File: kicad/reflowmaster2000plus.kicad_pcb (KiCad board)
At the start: 2 copper layers, 46.6 x 24.1 mm, 21 parts, among them IC1 TLP3063, P1 CONN_8, P2 Toaster, P3 220V, U1 TRIAC, U2 TLC2272

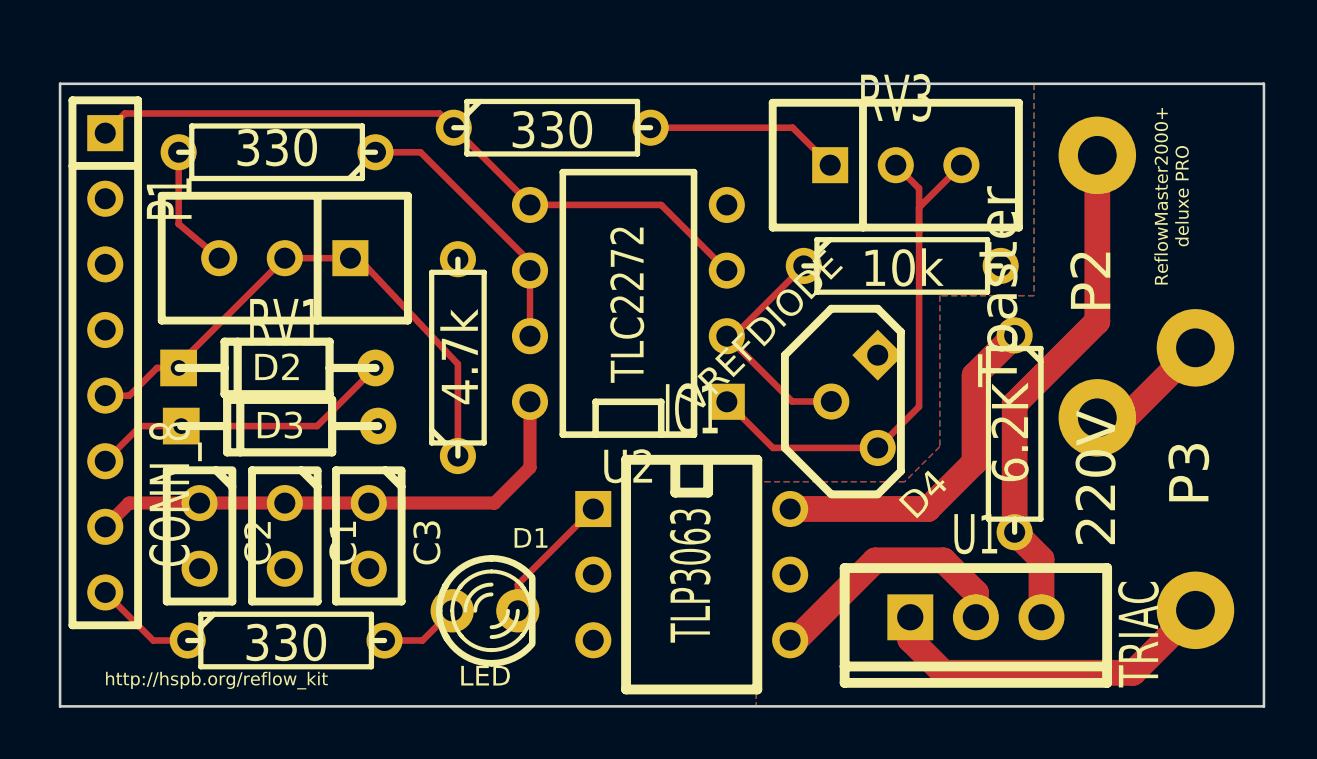
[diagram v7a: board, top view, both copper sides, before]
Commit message: SCH and PCB almost completely redrawn. Moved symbols and components to a separate lib.
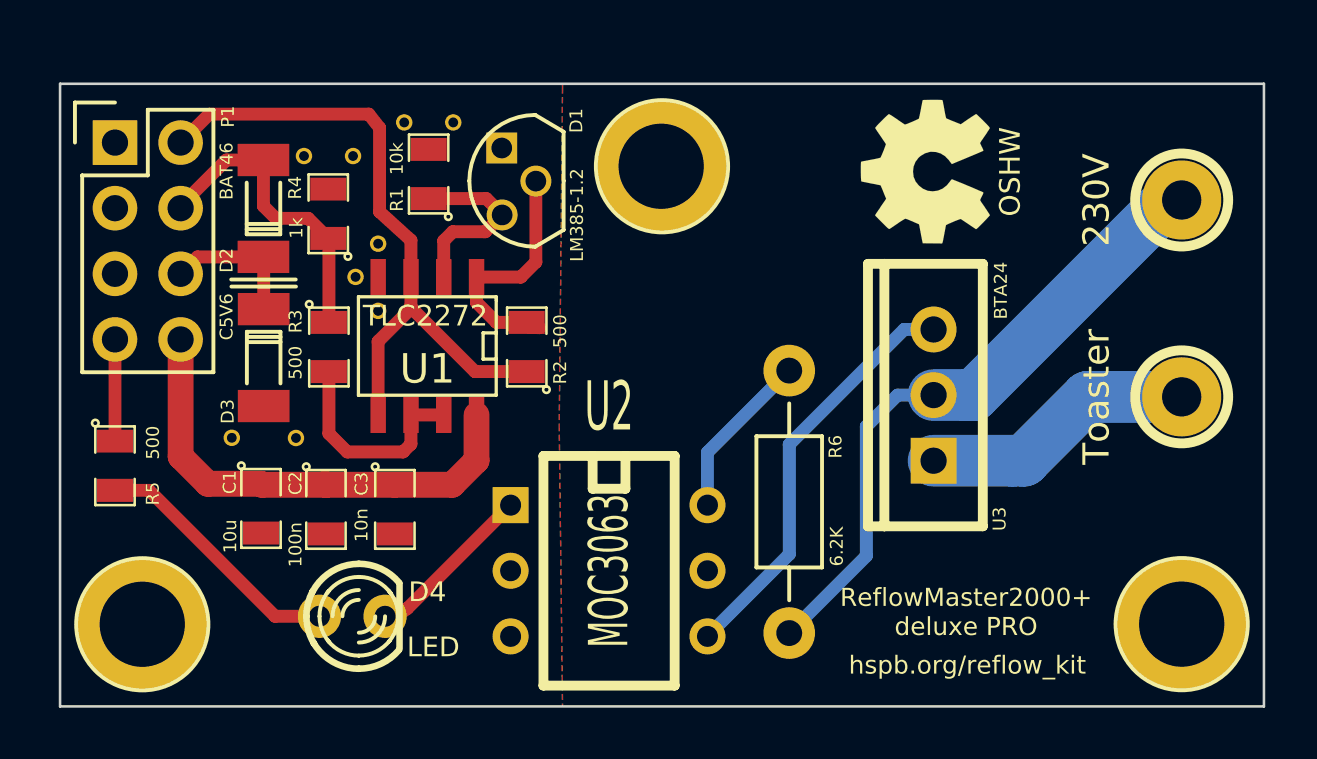
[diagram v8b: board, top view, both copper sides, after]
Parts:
- removed IC1: TLP3063, DIP-6__300
- removed R7: 330, R3
- removed RV1, RV3: 500, SIL-3
- added  : , acronet:oshw_logo_500, F.Cu at (188.6, 122.6)
- added 1Pin_15mil_VIA: VAL**, opendous:1Pin_15mil_VIA, F.Cu at (167.4, 128.0)
- added 1Pin_15mil_VIA: VAL**, opendous:1Pin_15mil_VIA, F.Cu at (168.4, 120.4)
- added 1Pin_15mil_VIA: VAL**, opendous:1Pin_15mil_VIA, F.Cu at (166.4, 122.0)
- added 1Pin_15mil_VIA: VAL**, opendous:1Pin_15mil_VIA, F.Cu at (166.5, 126.7)
- added 1Pin_15mil_VIA: VAL**, opendous:1Pin_15mil_VIA, F.Cu at (167.4, 125.4)
- added 1Pin_15mil_VIA: VAL**, opendous:1Pin_15mil_VIA, F.Cu at (170.3, 120.4)
- added 1Pin_15mil_VIA: VAL**, opendous:1Pin_15mil_VIA, F.Cu at (152.8, 131.2)
- added 1Pin_15mil_VIA: VAL**, opendous:1Pin_15mil_VIA, F.Cu at (164.2, 132.9)
- added 1Pin_15mil_VIA: VAL**, opendous:1Pin_15mil_VIA, F.Cu at (161.7, 132.9)
- added 1Pin_15mil_VIA: VAL**, opendous:1Pin_15mil_VIA, F.Cu at (164.5, 122.0)
- added 1Pin_15mil_VIA: VAL**, opendous:1Pin_15mil_VIA, F.Cu at (165.3, 116.7)
- added ?: , Connect:1pin, F.Cu at (198.5, 140.1)
- added ?: , Connect:1pin, F.Cu at (158.3, 140.1)
- added ?: , Connect:1pin, F.Cu at (178.4, 122.4)
- added R3: 500, rf2kpdp:SM0805-R, F.Cu at (165.5, 129.4)
- added U3: BTA24, rf2kpdp:TO220AB_BTA24, F.Cu at (188.9, 131.2)
- C1, C2, C3: footprint C1 -> rf2kpdp:SM0805-C
- D1: value LED -> LM385-1.2; footprint LED-3MM -> TO-92_LE33CZ
- D2: footprint DO-35 -> SOD-80
- D3: value BZX55C5V1 -> C5V6; footprint DO-35 -> rf2kpdp:SOD-80
- D4: value VREFDIODE -> LED; footprint TO92 -> rf2kpdp:LED-3MM
- P1: value CONN_8 -> CONN_02X04; footprint SIL-8 -> rf2kpdp:Pin_Header_Straight_2x04
- P2: value Toaster -> 230V; footprint WireConnection_1-5mmDrill -> rf2kpdp:1pin-small
- P3: value 220V -> Toaster; footprint WireConnection_1-5mmDrill -> rf2kpdp:1pin-small
- R1: value 6.2K -> 10k; footprint R3 -> rf2kpdp:SM0805-R
- R2: value 330 -> 500; footprint R3 -> rf2kpdp:SM0805-R
- R4: value 330 -> 1k; footprint R3 -> rf2kpdp:SM0805-R
- R5: value 4.7k -> 500; footprint R3 -> rf2kpdp:SM0805-R
- R6: value 10k -> 6.2K; footprint R3 -> rf2kpdp:Resistor_Horizontal_RM10mm
- U1: value TRIAC -> TLC2272; footprint TO220_VERT -> rf2kpdp:SO8E
- U2: value TLC2272 -> MOC3063; footprint DIP-8__300 -> rf2kpdp:DIP-6__300
- moved R1 24.8 mm to (169.4, 122.7), turned to 90 degrees
- moved U1 23.7 mm to (169.3, 129.3), turned to 180 degrees
- moved D4 22.0 mm to (166.4, 139.8), turned to 0 degrees
- moved D1 16.8 mm to (173.5, 123.0), turned to 90 degrees
- moved R4 16.6 mm to (165.5, 124.2), turned to 90 degrees
- moved R5 13.9 mm to (157.2, 134.0), turned to 270 degrees
- moved R2 12.3 mm to (173.2, 129.4), turned to 90 degrees
- moved U2 10.4 mm to (176.3, 138.1), turned to 270 degrees
- moved R6 10.1 mm to (183.3, 135.4), turned to 270 degrees
- moved P1 8.53 mm to (157.2, 121.5), turned to 0 degrees
- moved D2 6.20 mm to (163.0, 124.0), turned to 90 degrees
- moved C2 5.00 mm to (165.4, 135.7)
- moved P2 4.68 mm to (198.5, 123.7)
- moved P3 3.23 mm to (198.5, 131.3)
- moved D3 2.72 mm to (163.0, 129.8), turned to 270 degrees
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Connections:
- D1 pad 1: N-000006 -> (no net)
- D1 pad 2: N-000005 -> Net-(D1-Pad2)
- D3 pad 1: GND -> /Uclamp
- D3 pad 2: /Uclamp -> GND
- D4 pad 1: (no net) -> Net-(D4-Pad1)
- D4 pad 2: N-0000011 -> Net-(D4-Pad2)
- P1 pad 1: /KTYa -> GND
- P1 pad 2: GND -> /KTYa
- P1 pad 4: GND -> /Utemp
- P1 pad 5: /Utemp -> GND
- P1 pad 7: +12V -> /PWRctrl
- P1 pad 8: /PWRctrl -> +12V
- P2 pad 1: N-0000018 -> Net-(P2-Pad1)
- P3 pad 1: GNDPWR -> Net-(P3-Pad1)
- R1 pad 1: N-000007 -> Net-(D1-Pad3)
- R1 pad 2: N-0000018 -> GND
- R2 pad 1: N-000003 -> /KTYa
- R2 pad 2: N-0000013 -> Net-(D1-Pad2)
- R4 pad 1: /PWRctrl -> /Utemp
- R4 pad 2: N-000006 -> GND
- R5 pad 1: /Utemp -> /PWRctrl
- R5 pad 2: GND -> Net-(D4-Pad1)
- R6 pad 1: N-0000011 -> Net-(R6-Pad1)
- R6 pad 2: GND -> Net-(P2-Pad1)
- U1 pad 1: N-0000010 -> Net-(D1-Pad2)
- U1 pad 2: N-0000018 -> Net-(D1-Pad3)
- U1 pad 3: N-000009 -> /KTYa
- U2 pad 1: N-0000016 -> Net-(D4-Pad2)
- U2 pad 2: N-0000011 -> GND
- U2 pad 3: /KTYa -> (no net)
- U2 pad 4: GND -> Net-(U2-Pad4)
- U2 pad 5: /KTYa -> (no net)
- U2 pad 6: N-000003 -> Net-(R6-Pad1)
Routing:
- net Net-(P2-Pad1): track 0.00 -> 24.6 mm
- net N-0000016: track 21.8 -> 0.00 mm
- net N-0000018: track 19.6 -> 0.00 mm
- net Net-(U2-Pad4): track 0.00 -> 16.2 mm
- net N-000007: track 13.5 -> 0.00 mm
- net N-0000010: track 13.4 -> 0.00 mm
- net N-000003: track 10.6 -> 0.00 mm
- net Net-(D1-Pad2): track 0.00 -> 9.98 mm
- net N-000009: track 9.94 -> 0.00 mm
- net Net-(D4-Pad1): track 0.00 -> 9.93 mm
- net Net-(P3-Pad1): track 0.00 -> 9.91 mm
- net N-0000011: track 9.20 -> 0.00 mm
- net /Utemp: track 21.3 -> 12.6 mm
- net Net-(R3-Pad2): track 0.00 -> 8.41 mm
- net N-0000017: track 7.55 -> 0.00 mm
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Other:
- net class Default: trace_width 0.254 -> 0.5
- net class hvpwr: trace_width 1 -> 2
- net class hvpwrlc added: clearance 0.254, trace_width 1, via_dia 0.889, via_drill 0.635
- net class pwr: trace_width 0.508 -> 1
- board text added: "hspb.org/reflow_kit"
- board text removed: "http://hspb.org/reflow_kit"
